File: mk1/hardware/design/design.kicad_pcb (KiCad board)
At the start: 2 copper layers, 50 x 80 mm, 34 parts, among them U1 Teensy4.1, U10 LIS2MDL, U11 TBC05-04, U12 TBC05-04, U2 HM-TRP-868, U3 BMP390, U4 LSM6DSV80X, U5 D30V30MAL, U6 L80-R, U7 VN5E160STR, U8 VN5E160STR, U9 TBC05-04

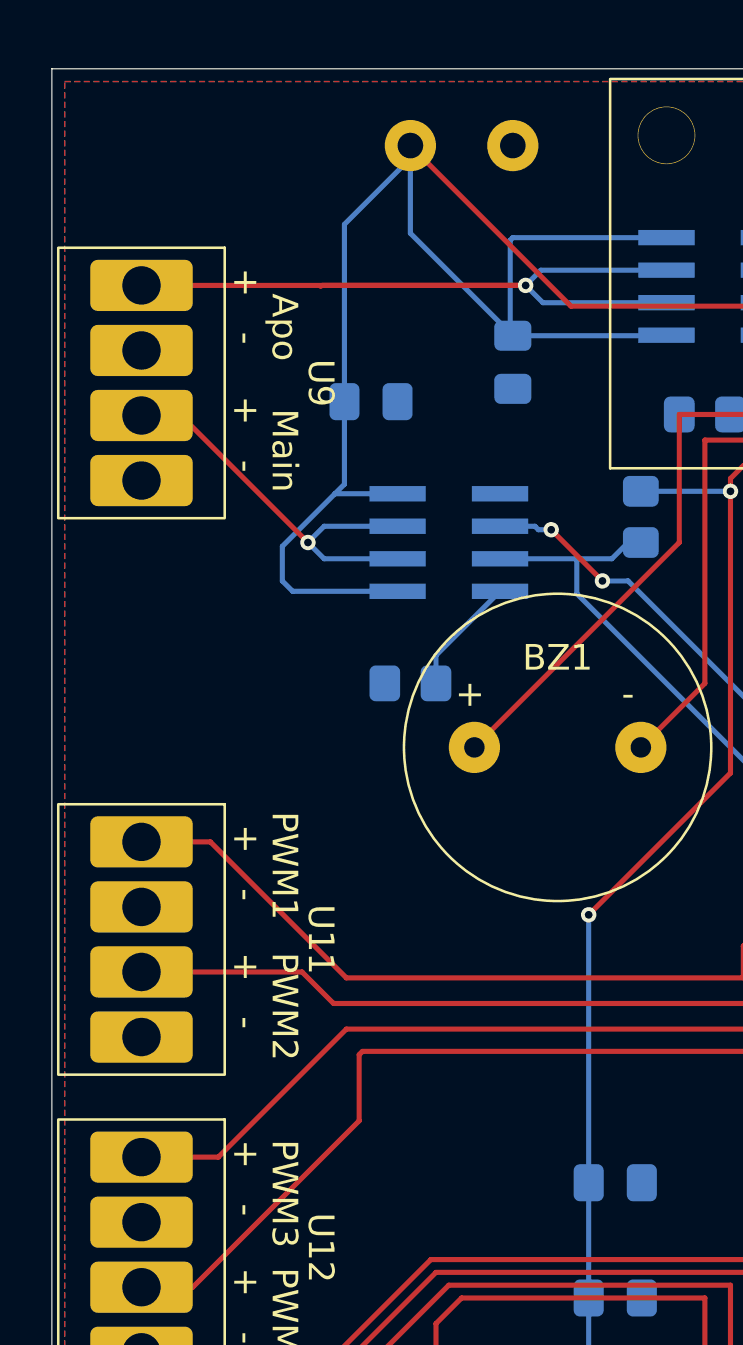
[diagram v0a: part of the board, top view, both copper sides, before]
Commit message: Added mounting holes
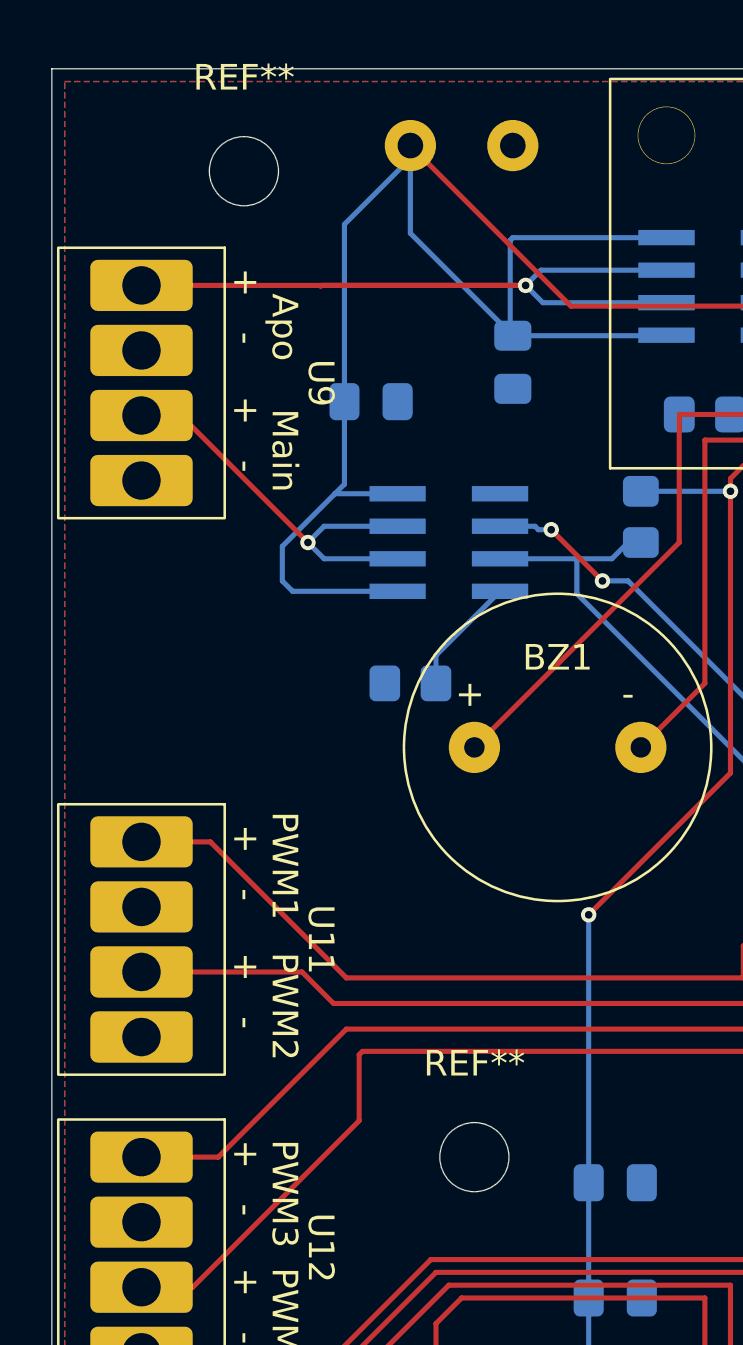
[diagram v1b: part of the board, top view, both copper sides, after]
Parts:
- added REF**: MountingHole_2.7mm_M2.5, MountingHole:MountingHole_2.7mm_M2.5, F.Cu at (87.5, 88.5)
- added REF**: MountingHole_2.7mm_M2.5, MountingHole:MountingHole_2.7mm_M2.5, F.Cu at (78.5, 50.0)
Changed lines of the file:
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@@
+		(embedded_fonts no)
+	)
+	(footprint "MountingHole:MountingHole_2.7mm_M2.5"
+		(layer "F.Cu")
+		(at 87.5 88.5)
+		(descr "Mounting Hole 2.7mm, M2.5, no annular, generated by kicad-footprint-generator mountinghole.py")
+		(tags "mountinghole M2.5")
+		(property "Reference" "REF**"
+			(at 0 -3.65 0)
+			(layer "F.SilkS")
+			(effects
+				(font
+					(size 1 1)
+					(thickness 0.15)
+				)
+			)
+		)
+		(property "Value" "MountingHole_2.7mm_M2.5"
+			(at 0 3.65 0)
+			(layer "F.Fab")
+			(effects
+				(font
+					(size 1 1)
+					(thickness 0.15)
+				)
+			)
+		)
+		(property "Datasheet" ""
+			(at 0 0 0)
+			(layer "F.Fab")
+			(hide yes)
+			(effects
+				(font
+					(size 1.27 1.27)
+					(thickness 0.15)
+				)
+			)
+		)
+		(property "Description" ""
+			(at 0 0 0)
+			(layer "F.Fab")
+			(hide yes)
+			(effects
+				(font
+					(size 1.27 1.27)
+					(thickness 0.15)
+				)
+			)
+		)
+		(attr exclude_from_pos_files exclude_from_bom)
+		(fp_circle
+			(center 0 0)
+			(end 2.7 0)
+			(stroke
+				(width 0.15)
+				(type solid)
+			)
+			(fill no)
+			(layer "Cmts.User")
+		)
+		(fp_circle
+			(center 0 0)
+			(end 2.95 0)
+			(stroke
+				(width 0.05)
+				(type solid)
+			)
+			(fill no)
+			(layer "F.CrtYd")
+		)
+		(fp_text user "${REFERENCE}"
+			(at 0 0 0)
+			(layer "F.Fab")
+			(effects
+				(font
+					(size 1 1)
+					(thickness 0.15)
+				)
+			)
+		)
+		(pad "" np_thru_hole circle
+			(at 0 0)
+			(size 2.7 2.7)
+			(drill 2.7)
+			(layers "*.Cu" "*.Mask")
+		)
 		(embedded_fonts no)
 	)
@@
 		)
 	)
+	(footprint "MountingHole:MountingHole_2.7mm_M2.5"
+		(layer "F.Cu")
+		(at 78.5 50)
+		(descr "Mounting Hole 2.7mm, M2.5, no annular, generated by kicad-footprint-generator mountinghole.py")
+		(tags "mountinghole M2.5")
+		(property "Reference" "REF**"
+			(at 0 -3.65 0)
+			(layer "F.SilkS")
+			(effects
+				(font
+					(size 1 1)
+					(thickness 0.15)
+				)
+			)
+		)
+		(property "Value" "MountingHole_2.7mm_M2.5"
+			(at 0 3.65 0)
+			(layer "F.Fab")
+			(effects
+				(font
+					(size 1 1)
+					(thickness 0.15)
+				)
+			)
+		)
+		(property "Datasheet" ""
+			(at 0 0 0)
+			(layer "F.Fab")
+			(hide yes)
+			(effects
+				(font
+					(size 1.27 1.27)
+					(thickness 0.15)
+				)
+			)
+		)
+		(property "Description" ""
+			(at 0 0 0)
+			(layer "F.Fab")
+			(hide yes)
+			(effects
+				(font
+					(size 1.27 1.27)
+					(thickness 0.15)
+				)
+			)
+		)
+		(attr exclude_from_pos_files exclude_from_bom)
+		(fp_circle
+			(center 0 0)
+			(end 2.7 0)
+			(stroke
+				(width 0.15)
+				(type solid)
+			)
+			(fill no)
+			(layer "Cmts.User")
+		)
+		(fp_circle
+			(center 0 0)
+			(end 2.95 0)
+			(stroke
+				(width 0.05)
+				(type solid)
+			)
+			(fill no)
+			(layer "F.CrtYd")
+		)
+		(fp_text user "${REFERENCE}"
+			(at 0 0 0)
+			(layer "F.Fab")
+			(effects
+				(font
+					(size 1 1)
+					(thickness 0.15)
+				)
+			)
+		)
+		(pad "" np_thru_hole circle
+			(at 0 0)
+			(size 2.7 2.7)
+			(drill 2.7)
+			(layers "*.Cu" "*.Mask")
+		)
+		(embedded_fonts no)
+	)
 	(footprint "missing_footprints:TBC05-04_pwm2"

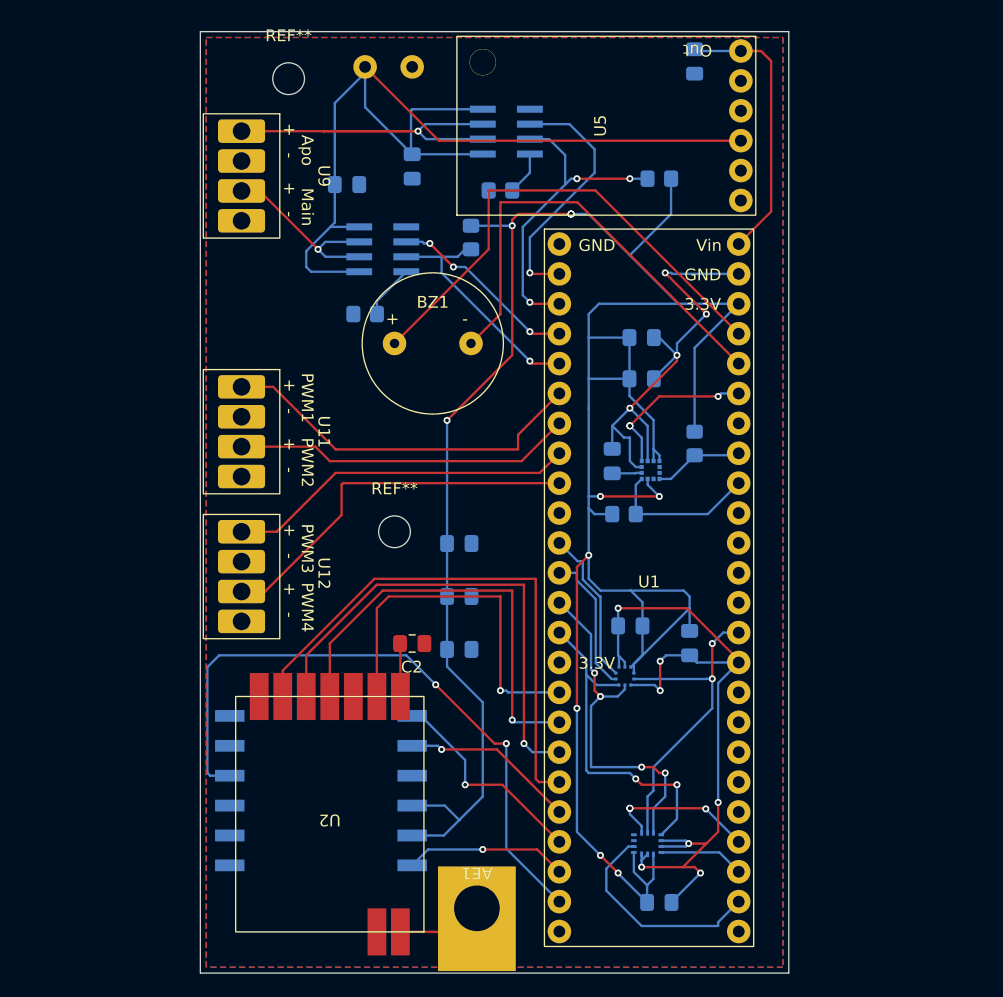
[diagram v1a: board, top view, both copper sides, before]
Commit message: Thickened power traces, and tidied up a few sections. Still a bunch of design rule errors to work through
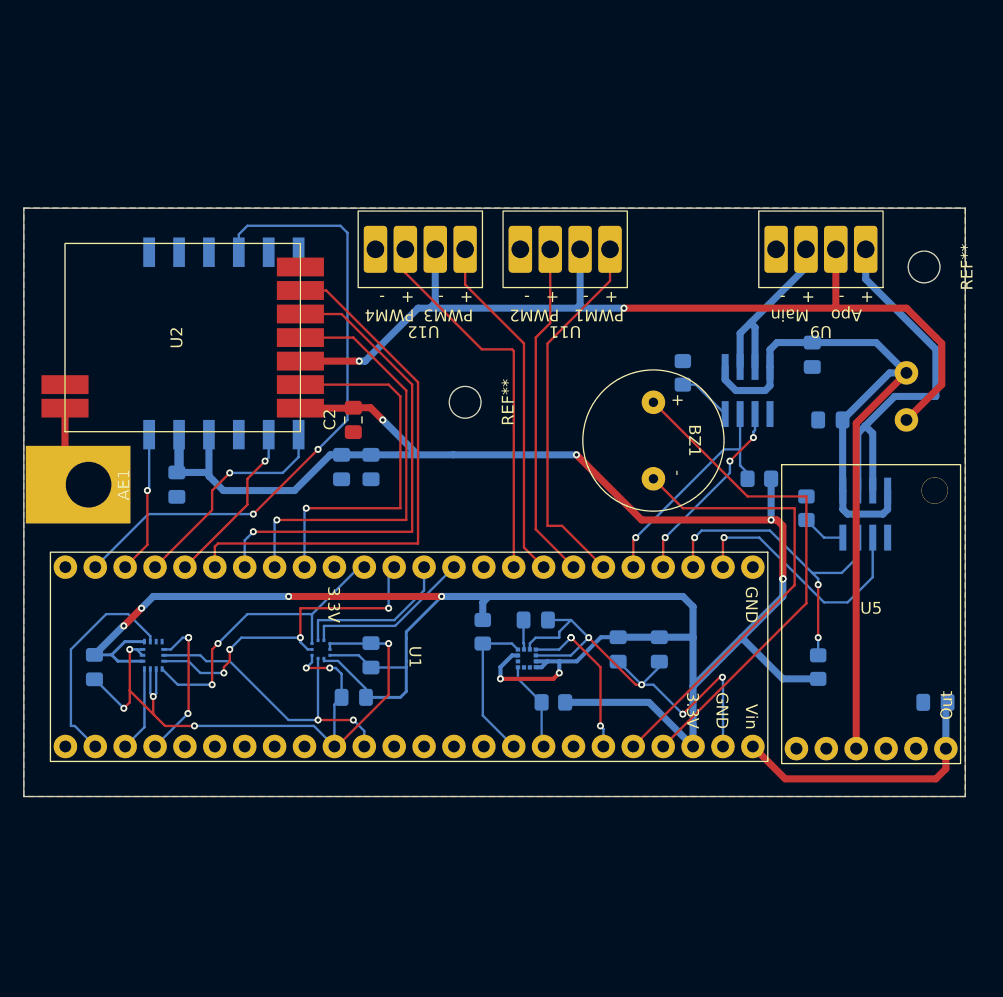
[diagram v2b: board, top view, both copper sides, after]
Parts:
- moved C1 58.2 mm to (133.5, 103.0), turned to 180 degrees
- moved REF** 56.3 mm to (132.5, 66.0), turned to -90 degrees
- moved U13 52.2 mm to (131.0, 77.0), turned to -90 degrees
- moved C5 52.0 mm to (62.0, 100.0), turned to -90 degrees
- moved U9 49.6 mm to (123.7, 64.5), turned to 180 degrees
- moved U5 47.2 mm to (128.0, 95.5), turned to 0 degrees
- moved U4 44.9 mm to (67.0, 99.0), turned to 90 degrees
- moved U7 44.6 mm to (127.5, 87.0), turned to 180 degrees
- moved R4 43.6 mm to (123.5, 100.0), turned to 90 degrees
- moved U2 42.4 mm to (69.5, 72.0), turned to 90 degrees
- moved C13 42.1 mm to (123.0, 73.5), turned to -90 degrees
- moved C12 41.6 mm to (124.5, 79.0), turned to 180 degrees
- moved AE1 39.7 mm to (68.0, 84.5), turned to 90 degrees
- moved U6 38.3 mm to (73.5, 72.5), turned to 90 degrees
- moved R1 37.5 mm to (122.5, 86.5), turned to -90 degrees
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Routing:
- net GND: track 108.7 -> 185.1 mm, vias 11 -> 13
- net +7.4V: track 85.9 -> 75.9 mm
- net /MISO: track 28.9 -> 26.2 mm
- net +3V3: track 243.1 -> 241.0 mm, vias 10 -> 11
- net /GPS-RST: track 55.2 -> 53.3 mm
- net /GPS-1PPS: track 13.8 -> 12.1 mm
- net /MAIN-OUT: track 16.1 -> 17.8 mm, vias 1 -> 0
- net /BMP-CS: track 12.1 -> 13.8 mm
- net /SCK: track 27.7 -> 26.2 mm
- net /MOSI: track 30.5 -> 29.4 mm
- net /APO-OUT: track 34.5 -> 33.5 mm, vias 1 -> 0
- net /BMP-INT: track 13.4 -> 14.4 mm
- net /GPS-RX: track 18.2 -> 18.9 mm
- net /GPS-TX: track 14.8 -> 14.2 mm
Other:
- board size 50 x 80 mm -> 80 x 50 mm

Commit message: Fixed errors and some warnings
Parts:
- removed REF** (x2): MountingHole_2.7mm_M2.5, MountingHole:MountingHole_2.7mm_M2.5
- added H1: MountingHole, MountingHole:MountingHole_2.7mm_M2.5, F.Cu at (132.5, 66.0)
- added H2: MountingHole, MountingHole:MountingHole_2.7mm_M2.5, F.Cu at (93.5, 77.5)
- moved AE1 0.71 mm to (68.5, 85.0)
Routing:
- net GND: track 185.1 -> 205.6 mm, vias 13 -> 16
- net /GPS-1PPS: track 12.1 -> 12.8 mm
- net +3V3: track 241.0 -> 240.9 mm, vias 11 -> 10
- net /MAG-DRDY: vias 3 -> 2
- net /IMU-CS: vias 3 -> 2
